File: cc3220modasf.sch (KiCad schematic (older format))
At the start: 110 parts, among them J1 Conn_02x10_Odd_Even, J10 Conn_01x02, J12 Conn_02x03_Odd_Even, J13 Conn_02x05_Counter_Clockwise, J14 Conn_01x02, J15 Conn_01x02, J16 Conn_01x02, J18 Conn_01x02, J19 Conn_01x02, J2 Conn_02x10_Odd_Even, J20 Conn_01x02, J21 Conn_01x03, J22 Conn_01x03, J26 Conn_01x03, J3 Conn_02x06_Odd_Even, J5 Conn_01x03, J6 Conn_01x03, J7 Conn_02x07_Odd_Even, J9 Conn_01x02, Q4 BSS138, Q5 TP0610T, Q6 BSS138, Q7 BSS138, SW2 SW_DIP_x01, U10 TMP006AIYZFR, U7 OPA4340UA, U9 CC3220MODASF12MONR

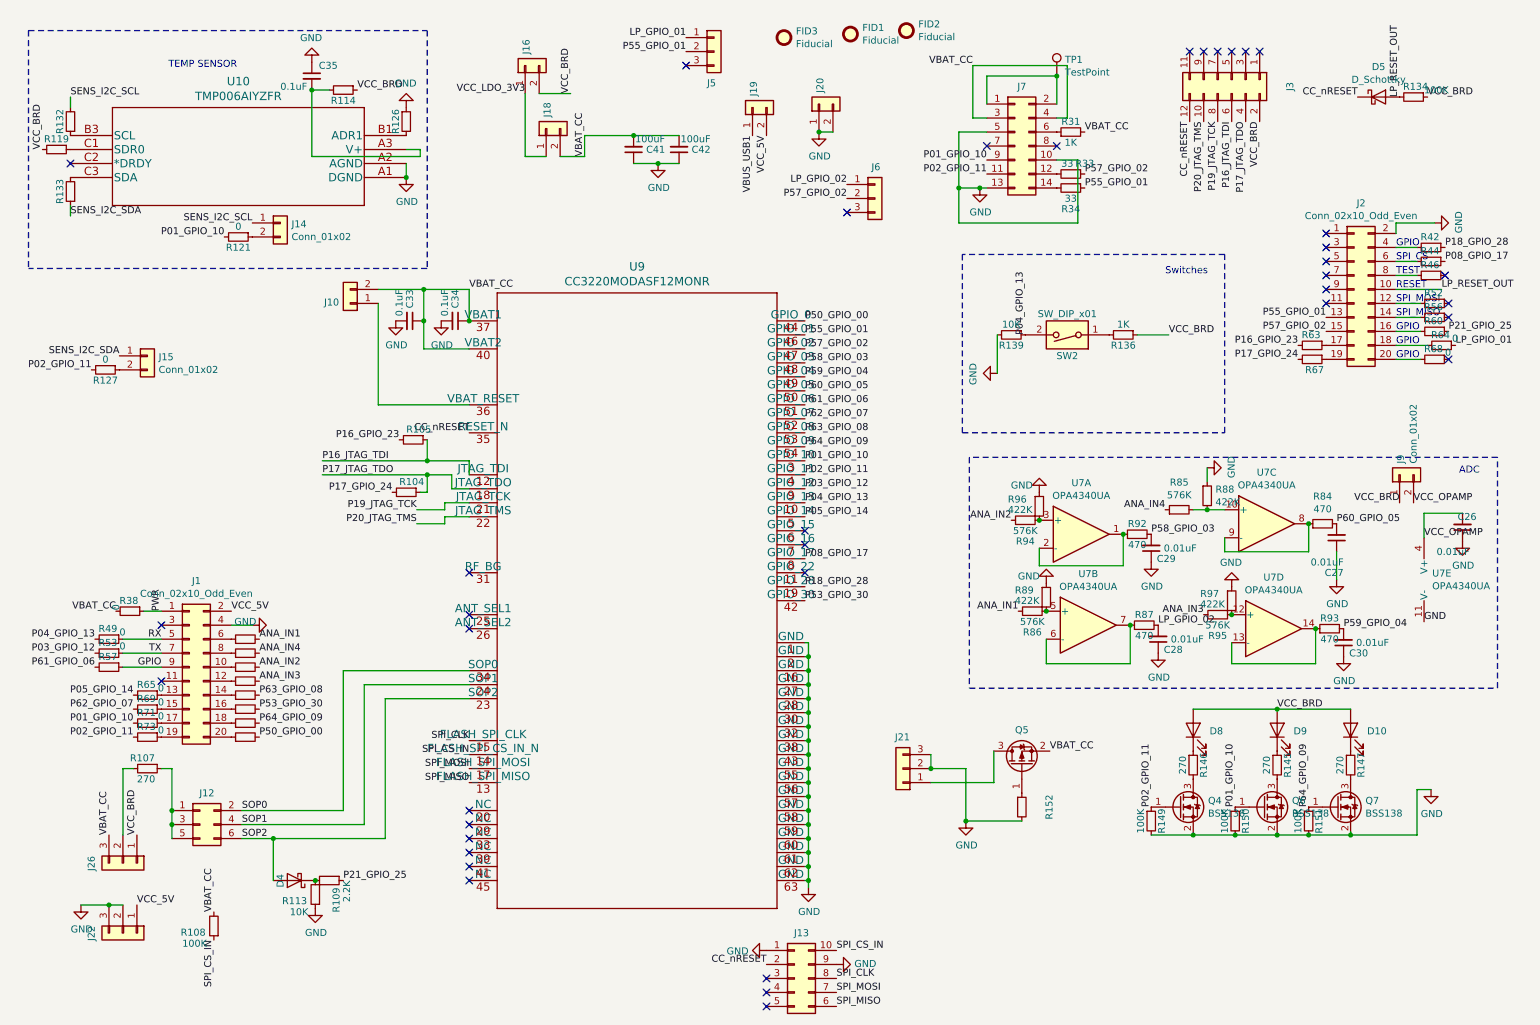
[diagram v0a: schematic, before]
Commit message: Reduced board size to 49mmx57mm. Headers should now match pwrcon_1 commit from similar date
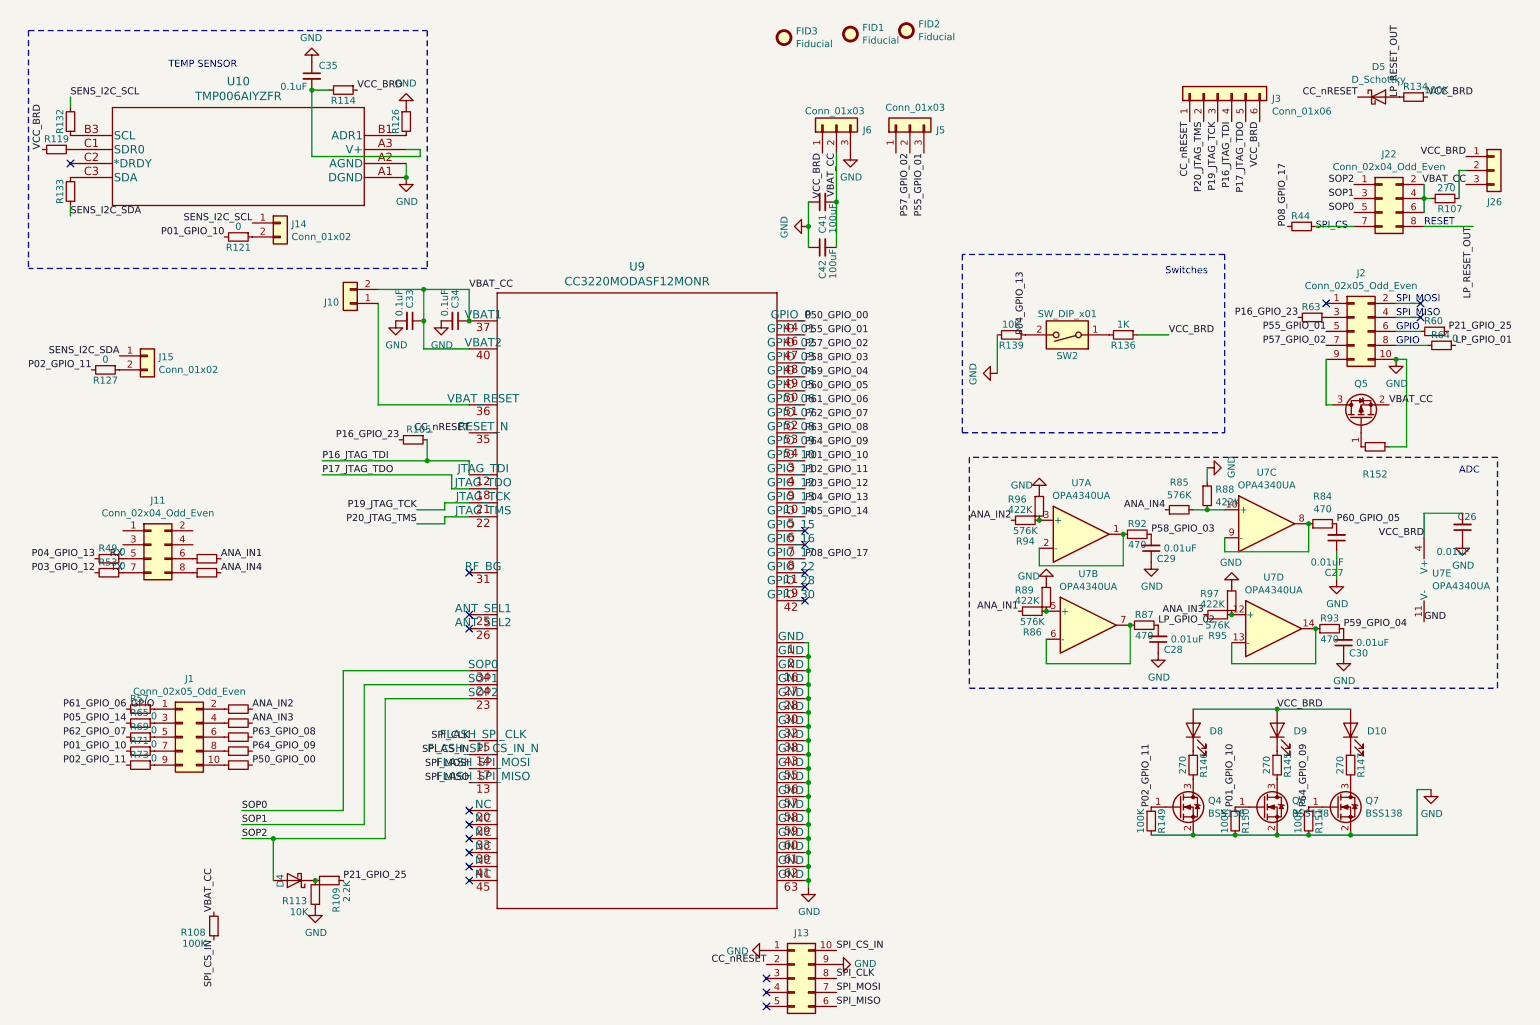
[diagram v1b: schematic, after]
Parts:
- removed J1, J2: Conn_02x10_Odd_Even, Connector_PinHeader_2.54mm:PinHeader_2x10_P2.54mm_Vertical, symbol Connector_Generic:Conn_02x10_Odd_Even
- removed J12: Conn_02x03_Odd_Even, Connector_PinHeader_2.54mm:PinHeader_2x03_P2.54mm_Vertical, symbol Connector_Generic:Conn_02x03_Odd_Even
- removed J16, J18, J19, J20, J9: Conn_01x02, Connector_PinHeader_2.54mm:PinHeader_1x02_P2.54mm_Vertical, symbol Connector_Generic:Conn_01x02
- removed J21, J22: Conn_01x03, Connector_PinHeader_2.54mm:PinHeader_1x03_P2.54mm_Vertical, symbol Connector_Generic:Conn_01x03
- removed J3: Conn_02x06_Odd_Even, Connector_PinSocket_2.54mm:PinSocket_2x06_P2.54mm_Vertical, symbol Connector_Generic:Conn_02x06_Odd_Even
- removed J7: Conn_02x07_Odd_Even, Connector_PinHeader_1.27mm:PinHeader_2x07_P1.27mm_Vertical_SMD, symbol Connector_Generic:Conn_02x07_Odd_Even
- removed R104, R42, R46, R52, R56, R67, R68, R70: 0, Resistor_SMD:R_0402_1005Metric, symbol Device:R_Small
- removed R31: 1K, Resistor_SMD:R_0402_1005Metric, symbol Device:R_Small
- removed R33, R34: 33, Resistor_SMD:R_0603_1608Metric, symbol Device:R_Small
- removed R38: 0, Resistor_SMD:R_0603_1608Metric, symbol Device:R_Small
- removed TP1: TestPoint, TestPoint:TestPoint_Pad_D2.0mm, symbol Connector:TestPoint
- added J1, J2: Conn_02x05_Odd_Even, Connector_PinHeader_2.54mm:PinHeader_2x05_P2.54mm_Vertical, symbol Connector_Generic:Conn_02x05_Odd_Even
- added J11, J22: Conn_02x04_Odd_Even, Connector_PinHeader_2.54mm:PinHeader_2x04_P2.54mm_Vertical, symbol Connector_Generic:Conn_02x04_Odd_Even
- added J3: Conn_01x06, Connector_PinSocket_2.54mm:PinSocket_1x06_P2.54mm_Vertical, symbol Connector_Generic:Conn_01x06
- J5, J6: MFG Name Wurth Elektronik -> (none); MFG Part Num '61300311121 -> (none)
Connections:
- net VCC_OPAMP is gone; now on net VCC_BRD: C26.2, U7.4 (V+)
- net CC_nRESET: now also J3.1 (Pin_1)
- net GND: now also J6.3 (Pin_3), R152.1, J2.10 (Pin_10); no longer R152.2
- net GPIO: now also J1.1 (Pin_1)
- net LP_GPIO_01: no longer J5.1 (Pin_1)
- net LP_GPIO_02: no longer J6.1 (Pin_1)
- net LP_RESET_OUT: now also J22.8 (Pin_8)
- net P08_GPIO_17: now also R44.2; no longer R44.1
- net P16_JTAG_TDI: now also J3.4 (Pin_4)
- net P17_JTAG_TDO: now also J3.5 (Pin_5)
- net P19_JTAG_TCK: now also J3.3 (Pin_3)
- net P20_JTAG_TMS: now also J3.2 (Pin_2)
- net P55_GPIO_01: now also J5.3 (Pin_3), J2.5 (Pin_5); no longer J5.2 (Pin_2)
- net P57_GPIO_02: now also J5.2 (Pin_2), J2.7 (Pin_7); no longer J6.2 (Pin_2)
- net RX: now also J11.5 (Pin_5)
- net SOP0: now also J22.5 (Pin_5)
- net SOP1: now also J22.3 (Pin_3)
- net SOP2: now also J22.1 (Pin_1)
- net TX: now also J11.7 (Pin_7)
- net VBAT_CC: now also J6.2 (Pin_2)
- net VCC_BRD: now also J6.1 (Pin_1), J3.6 (Pin_6)
- net at Q5.3 (D): now also J2.9 (Pin_9)
- net at R50.1: now also J11.6 (Pin_6)
- net at R54.1: now also J11.8 (Pin_8)
- net at R58.1: now also J1.2 (Pin_2)
- net at R62.1: now also J1.4 (Pin_4)
- net at R66.1: now also J1.6 (Pin_6)
- net at R72.1: now also J1.8 (Pin_8)
- net at R74.1: now also J1.10 (Pin_10)
- net at Q5.1 (G): now also R152.2; no longer R152.1
- net at R107.1: now also J22.2 (Pin_2), J22.4 (Pin_4), J22.6 (Pin_6)
- net at R65.1: now also J1.3 (Pin_3)
- net at R69.1: now also J1.5 (Pin_5)
- net at R71.1: now also J1.7 (Pin_7)
- net at R73.1: now also J1.9 (Pin_9)
- net at R64.2: now also J2.8 (Pin_8)
- net at R60.2: now also J2.6 (Pin_6)
- net at R63.1: now also J2.3 (Pin_3)
- net P18_GPIO_28: no longer names the net of U9.19 (GPIO_28)
- net P53_GPIO_30: no longer names the net of U9.42 (GPIO_30)
- new net: J22.7 (Pin_7), R44.1
- no-connect marks 38 -> 21
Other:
- note removed: "TEST"
- moved on the sheet: C41, C42, J26, Q5, R107, R152, R44, R49, R53, R57, R63, R65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
